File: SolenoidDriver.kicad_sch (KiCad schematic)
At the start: 3 parts, among them Q1 DMN3731U-7

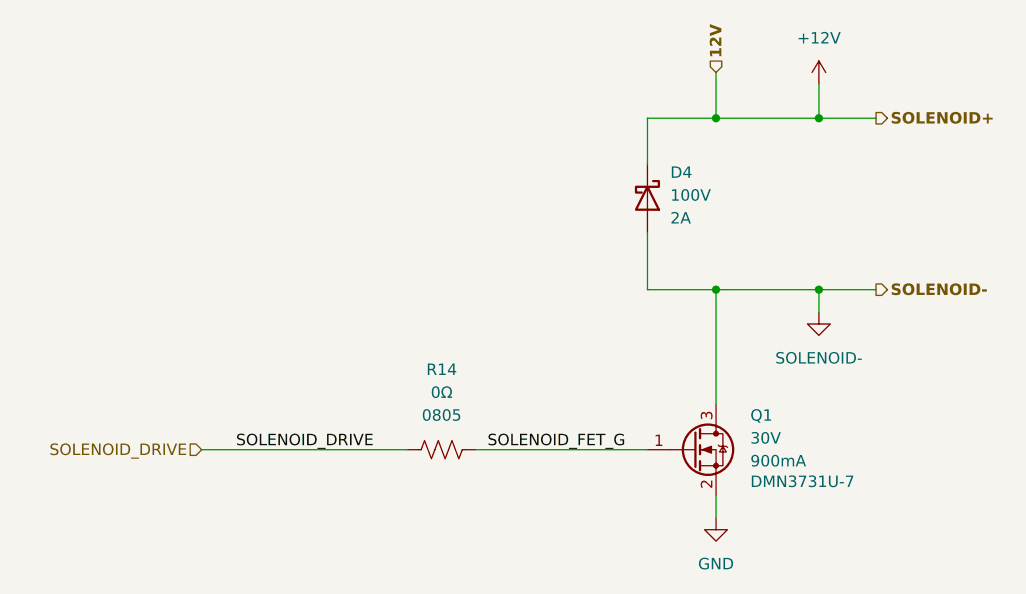
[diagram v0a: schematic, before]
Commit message: 1st round of rough component placement
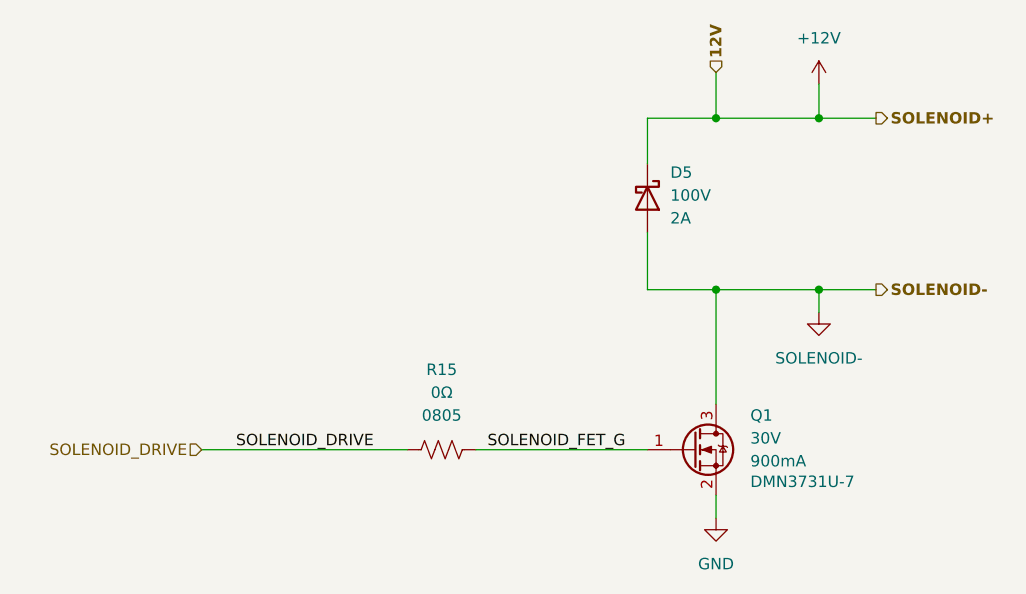
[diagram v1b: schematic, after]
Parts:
- renumbered D4 to D5, R14 to R15
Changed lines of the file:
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@@
 		(dnp no)
 		(fields_autoplaced yes)
-		(property "Reference" "#PWR049"
+		(property "Reference" "#PWR052"
 			(at 133.35 88.9 0)
 			(effects
@@
 			(project ""
 				(path "/c4971751-18ba-42c0-933f-7e935423e3d9/09553296-4412-4340-b738-04baff363726"
-					(reference "#PWR049")
+					(reference "#PWR052")
 					(unit 1)
 				)
@@
 		(dnp no)
 		(fields_autoplaced yes)
-		(property "Reference" "D4"
+		(property "Reference" "D5"
 			(at 116.84 94.9324 0)
 			(effects
@@
 			(project ""
 				(path "/c4971751-18ba-42c0-933f-7e935423e3d9/09553296-4412-4340-b738-04baff363726"
-					(reference "D4")
+					(reference "D5")
 					(unit 1)
 				)
@@
 		(dnp no)
 		(fields_autoplaced yes)
-		(property "Reference" "#PWR051"
+		(property "Reference" "#PWR053"
 			(at 133.35 116.84 0)
 			(effects
@@
 			(project ""
 				(path "/c4971751-18ba-42c0-933f-7e935423e3d9/09553296-4412-4340-b738-04baff363726"
-					(reference "#PWR051")
+					(reference "#PWR053")
 					(unit 1)
 				)
@@
 		(dnp no)
 		(fields_autoplaced yes)
-		(property "Reference" "R14"
+		(property "Reference" "R15"
 			(at 91.44 116.84 90)
 			(effects
@@
 			(project ""
 				(path "/c4971751-18ba-42c0-933f-7e935423e3d9/09553296-4412-4340-b738-04baff363726"
-					(reference "R14")
+					(reference "R15")
 					(unit 1)
 				)
@@
 		(dnp no)
 		(fields_autoplaced yes)
-		(property "Reference" "#PWR048"
+		(property "Reference" "#PWR054"
 			(at 121.92 139.7 0)
 			(effects
@@
 			(project ""
 				(path "/c4971751-18ba-42c0-933f-7e935423e3d9/09553296-4412-4340-b738-04baff363726"
-					(reference "#PWR048")
+					(reference "#PWR054")
 					(unit 1)
 				)

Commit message: 2nd rev is done
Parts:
- renumbered D5 to D6, Q1 to Q2, R15 to R21
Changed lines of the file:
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@@
 		(on_board yes)
 		(dnp no)
-		(property "Reference" "Q1"
+		(property "Reference" "Q2"
 			(at 125.73 121.9199 0)
 			(effects
@@
 			(project ""
 				(path "/c4971751-18ba-42c0-933f-7e935423e3d9/09553296-4412-4340-b738-04baff363726"
-					(reference "Q1")
+					(reference "Q2")
 					(unit 1)
 				)
@@
 		(dnp no)
 		(fields_autoplaced yes)
-		(property "Reference" "#PWR052"
+		(property "Reference" "#PWR060"
 			(at 133.35 88.9 0)
 			(effects
@@
 			(project ""
 				(path "/c4971751-18ba-42c0-933f-7e935423e3d9/09553296-4412-4340-b738-04baff363726"
-					(reference "#PWR052")
+					(reference "#PWR060")
 					(unit 1)
 				)
@@
 		(dnp no)
 		(fields_autoplaced yes)
-		(property "Reference" "D5"
+		(property "Reference" "D6"
 			(at 116.84 94.9324 0)
 			(effects
@@
 			(project ""
 				(path "/c4971751-18ba-42c0-933f-7e935423e3d9/09553296-4412-4340-b738-04baff363726"
-					(reference "D5")
+					(reference "D6")
 					(unit 1)
 				)
@@
 		(dnp no)
 		(fields_autoplaced yes)
-		(property "Reference" "#PWR053"
+		(property "Reference" "#PWR061"
 			(at 133.35 116.84 0)
 			(effects
@@
 			(project ""
 				(path "/c4971751-18ba-42c0-933f-7e935423e3d9/09553296-4412-4340-b738-04baff363726"
-					(reference "#PWR053")
+					(reference "#PWR061")
 					(unit 1)
 				)
@@
 		(dnp no)
 		(fields_autoplaced yes)
-		(property "Reference" "R15"
+		(property "Reference" "R21"
 			(at 91.44 116.84 90)
 			(effects
@@
 			(project ""
 				(path "/c4971751-18ba-42c0-933f-7e935423e3d9/09553296-4412-4340-b738-04baff363726"
-					(reference "R15")
+					(reference "R21")
 					(unit 1)
 				)
@@
 		(dnp no)
 		(fields_autoplaced yes)
-		(property "Reference" "#PWR054"
+		(property "Reference" "#PWR062"
 			(at 121.92 139.7 0)
 			(effects
@@
 			(project ""
 				(path "/c4971751-18ba-42c0-933f-7e935423e3d9/09553296-4412-4340-b738-04baff363726"
-					(reference "#PWR054")
+					(reference "#PWR062")
 					(unit 1)
 				)

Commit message: generated backup schematic pdfs
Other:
- title: (none) -> EauRouge
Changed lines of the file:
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@@
 	(generator_version "8.0")
 	(paper "A4")
+	(title_block
+		(title "EauRouge")
+		(date "2025-01-29")
+		(rev "1")
+	)
 	(junction
 		(at 133.35 107.95)
